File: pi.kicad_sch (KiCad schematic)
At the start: 12 parts

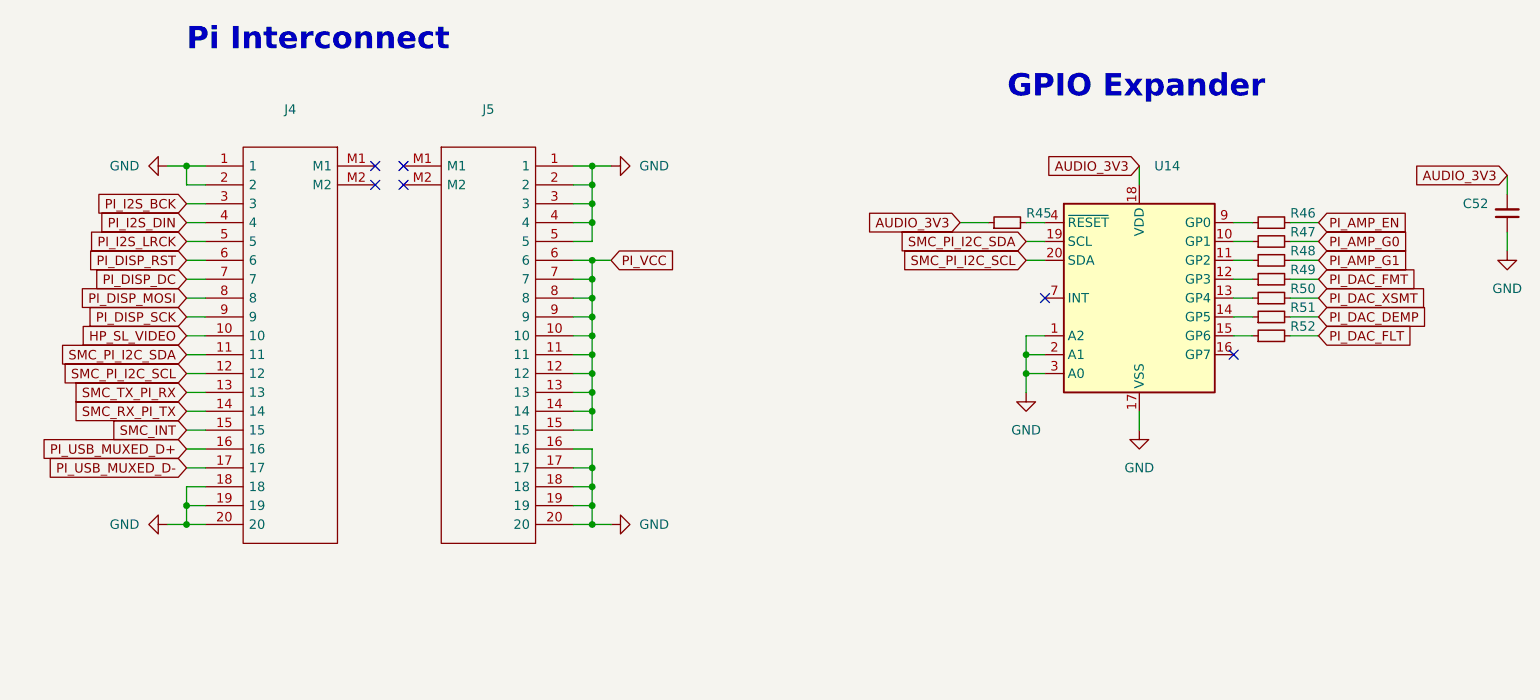
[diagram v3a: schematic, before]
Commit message: layout: update footprint for TP4056M
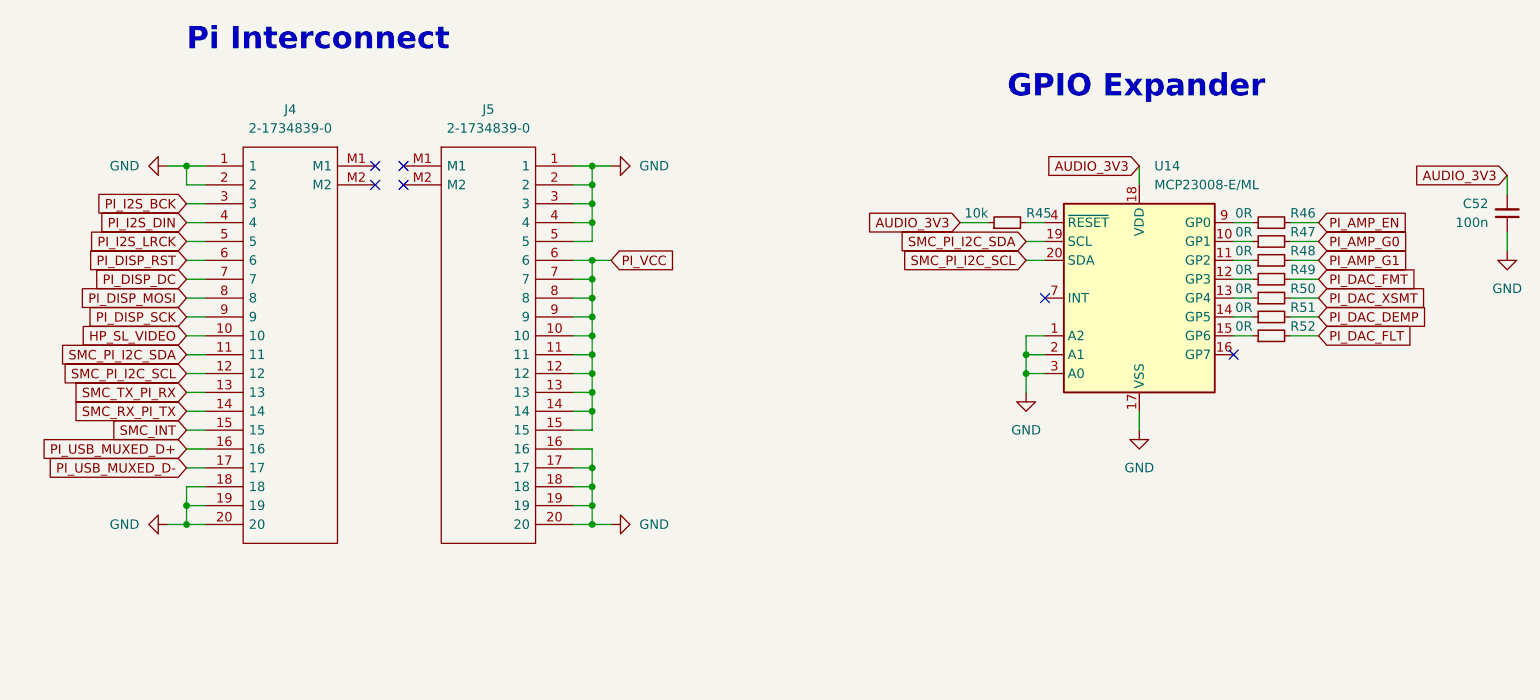
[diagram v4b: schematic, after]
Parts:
- C52: value (none) -> 100n; footprint (none) -> Capacitor_SMD:C_0402_1005Metric
- J4, J5: value (none) -> 2-1734839-0; footprint (none) -> Gigahawk:2-1734839-0
- R45: value (none) -> 10k; footprint (none) -> Resistor_SMD:R_0402_1005Metric
- R46, R47, R48, R49, R50, R51, R52: value (none) -> 0R; footprint (none) -> Resistor_SMD:R_0402_1005Metric
- U14: value (none) -> MCP23008-E/ML; footprint (none) -> Package_DFN_QFN:QFN-20-1EP_4x4mm_P0.5mm_EP2.7x2.7mm
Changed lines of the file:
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@@
       (effects (font (size 1.27 1.27)) (justify right))
     )
-    (property "Value" "" (id 1) (at 184.15 76.2 90)
-      (effects (font (size 1.27 1.27)) (justify left))
-    )
-    (property "Footprint" "" (id 2) (at 186.69 77.47 0)
+    (property "Value" "0R" (id 1) (at 184.15 76.2 90)
+      (effects (font (size 1.27 1.27)) (justify left))
+    )
+    (property "Footprint" "Resistor_SMD:R_0402_1005Metric" (id 2) (at 186.69 77.47 0)
       (effects (font (size 1.27 1.27)) hide)
     )
@@
       (effects (font (size 1.27 1.27)) (justify right))
     )
-    (property "Value" "" (id 1) (at 148.59 76.2 90)
-      (effects (font (size 1.27 1.27)) (justify left))
-    )
-    (property "Footprint" "" (id 2) (at 151.13 77.47 0)
+    (property "Value" "10k" (id 1) (at 148.59 76.2 90)
+      (effects (font (size 1.27 1.27)) (justify left))
+    )
+    (property "Footprint" "Resistor_SMD:R_0402_1005Metric" (id 2) (at 151.13 77.47 0)
       (effects (font (size 1.27 1.27)) hide)
     )
@@
       (effects (font (size 1.27 1.27)) (justify right))
     )
-    (property "Value" "" (id 1) (at 184.15 86.36 90)
-      (effects (font (size 1.27 1.27)) (justify left))
-    )
-    (property "Footprint" "" (id 2) (at 186.69 87.63 0)
+    (property "Value" "0R" (id 1) (at 184.15 86.36 90)
+      (effects (font (size 1.27 1.27)) (justify left))
+    )
+    (property "Footprint" "Resistor_SMD:R_0402_1005Metric" (id 2) (at 186.69 87.63 0)
       (effects (font (size 1.27 1.27)) hide)
     )
@@
       (effects (font (size 1.27 1.27)) (justify left))
     )
-    (property "Value" "" (id 1) (at 170.9294 72.39 0)
-      (effects (font (size 1.27 1.27)) (justify left))
-    )
-    (property "Footprint" "" (id 2) (at 168.91 114.3 0)
+    (property "Value" "MCP23008-E/ML" (id 1) (at 170.9294 72.39 0)
+      (effects (font (size 1.27 1.27)) (justify left))
+    )
+    (property "Footprint" "Package_DFN_QFN:QFN-20-1EP_4x4mm_P0.5mm_EP2.7x2.7mm" (id 2) (at 168.91 114.3 0)
       (effects (font (size 1.27 1.27)) hide)
     )
@@
     (in_bom yes) (on_board yes) (fields_autoplaced)
     (property "Reference" "J4" (id 0) (at 54.61 62.23 0))
-    (property "Value" "" (id 1) (at 54.61 64.77 0))
-    (property "Footprint" "" (id 2) (at 46.99 67.31 0)
+    (property "Value" "2-1734839-0" (id 1) (at 54.61 64.77 0))
+    (property "Footprint" "Gigahawk:2-1734839-0" (id 2) (at 46.99 67.31 0)
       (effects (font (size 1.27 1.27)) (justify left) hide)
     )
@@
     (in_bom yes) (on_board yes) (fields_autoplaced)
     (property "Reference" "J5" (id 0) (at 81.28 62.23 0))
-    (property "Value" "" (id 1) (at 81.28 64.77 0))
-    (property "Footprint" "" (id 2) (at 88.9 67.31 0)
+    (property "Value" "2-1734839-0" (id 1) (at 81.28 64.77 0))
+    (property "Footprint" "Gigahawk:2-1734839-0" (id 2) (at 88.9 67.31 0)
       (effects (font (size 1.27 1.27)) (justify left) hide)
     )
@@
       (effects (font (size 1.27 1.27)) (justify right))
     )
-    (property "Value" "" (id 1) (at 184.15 91.44 90)
-      (effects (font (size 1.27 1.27)) (justify left))
-    )
-    (property "Footprint" "" (id 2) (at 186.69 92.71 0)
+    (property "Value" "0R" (id 1) (at 184.15 91.44 90)
+      (effects (font (size 1.27 1.27)) (justify left))
+    )
+    (property "Footprint" "Resistor_SMD:R_0402_1005Metric" (id 2) (at 186.69 92.71 0)
       (effects (font (size 1.27 1.27)) hide)
     )
@@
       (effects (font (size 1.27 1.27)) (justify right))
     )
-    (property "Value" "" (id 1) (at 184.15 83.82 90)
-      (effects (font (size 1.27 1.27)) (justify left))
-    )
-    (property "Footprint" "" (id 2) (at 186.69 85.09 0)
+    (property "Value" "0R" (id 1) (at 184.15 83.82 90)
+      (effects (font (size 1.27 1.27)) (justify left))
+    )
+    (property "Footprint" "Resistor_SMD:R_0402_1005Metric" (id 2) (at 186.69 85.09 0)
       (effects (font (size 1.27 1.27)) hide)
     )
@@
       (effects (font (size 1.27 1.27)) (justify right))
     )
-    (property "Value" "" (id 1) (at 215.9 77.4635 0)
-      (effects (font (size 1.27 1.27)) (justify right))
-    )
-    (property "Footprint" "" (id 2) (at 218.44 76.2 0)
+    (property "Value" "100n" (id 1) (at 215.9 77.4635 0)
+      (effects (font (size 1.27 1.27)) (justify right))
+    )
+    (property "Footprint" "Capacitor_SMD:C_0402_1005Metric" (id 2) (at 218.44 76.2 0)
       (effects (font (size 1.27 1.27)) hide)
     )
@@
       (effects (font (size 1.27 1.27)) (justify right))
     )
-    (property "Value" "" (id 1) (at 184.15 88.9 90)
-      (effects (font (size 1.27 1.27)) (justify left))
-    )
-    (property "Footprint" "" (id 2) (at 186.69 90.17 0)
+    (property "Value" "0R" (id 1) (at 184.15 88.9 90)
+      (effects (font (size 1.27 1.27)) (justify left))
+    )
+    (property "Footprint" "Resistor_SMD:R_0402_1005Metric" (id 2) (at 186.69 90.17 0)
       (effects (font (size 1.27 1.27)) hide)
     )
@@
       (effects (font (size 1.27 1.27)) (justify right))
     )
-    (property "Value" "" (id 1) (at 184.15 78.74 90)
-      (effects (font (size 1.27 1.27)) (justify left))
-    )
-    (property "Footprint" "" (id 2) (at 186.69 80.01 0)
+    (property "Value" "0R" (id 1) (at 184.15 78.74 90)
+      (effects (font (size 1.27 1.27)) (justify left))
+    )
+    (property "Footprint" "Resistor_SMD:R_0402_1005Metric" (id 2) (at 186.69 80.01 0)
       (effects (font (size 1.27 1.27)) hide)
     )
@@
       (effects (font (size 1.27 1.27)) (justify right))
     )
-    (property "Value" "" (id 1) (at 184.15 81.28 90)
-      (effects (font (size 1.27 1.27)) (justify left))
-    )
-    (property "Footprint" "" (id 2) (at 186.69 82.55 0)
-      (effects (font (size 1.27 1.27)) hide)
-    )
+    (property "Value" "0R" (id 1) (at 184.15 81.28 90)
+      (effects (font (size 1.27 1.27)) (justify left))
+    )
+    (property "Footprint" "Resistor_SMD:R_0402_1005Metric" (id 2) (at 186.69 82.55 0)
+      (effects (font (size 1.27 1.27)) hide)
+    )

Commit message: layout: preliminary layout of most of board
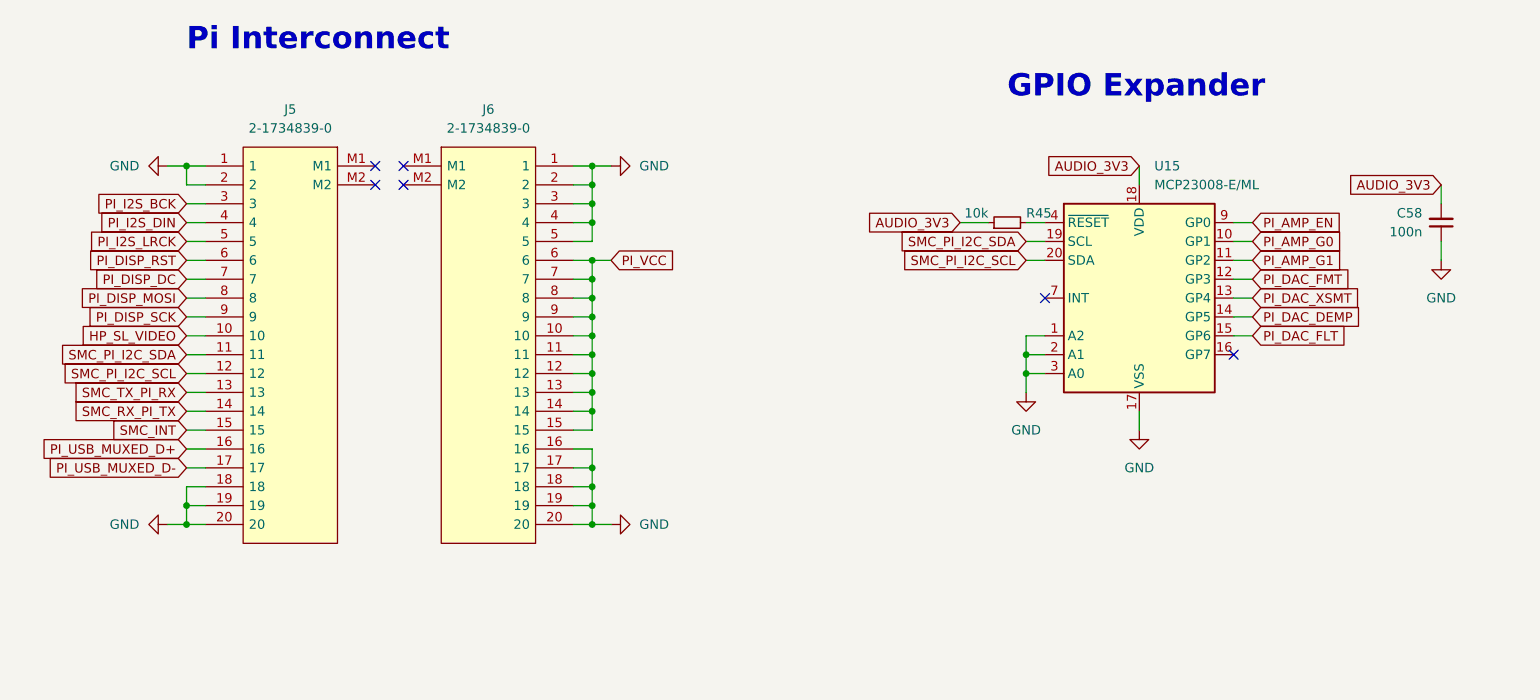
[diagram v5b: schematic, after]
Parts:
- removed R46, R47, R48, R49, R50, R51, R52: 0R, Resistor_SMD:R_0402_1005Metric, symbol Device:R_Small
- renumbered C52 to C58, J4 to J5, J5 to J6, U14 to U15
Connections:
- net PI_AMP_EN: now also U15.9 (GP0)
- net PI_AMP_G0: now also U15.10 (GP1)
- net PI_AMP_G1: now also U15.11 (GP2)
- net PI_DAC_DEMP: now also U15.14 (GP5)
- net PI_DAC_FLT: now also U15.15 (GP6)
- net PI_DAC_FMT: now also U15.12 (GP3)
- net PI_DAC_XSMT: now also U15.13 (GP4)
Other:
- moved on the sheet: C58

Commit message: routing: begin routing
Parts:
- removed J5, J6: 2-1734839-0, Gigahawk:2-1734839-0, symbol gigahawk:2-1734839-0
- added J5: (no value), symbol gigahawk:2-1734839-5
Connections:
- net GND: now also J5.24, J5.25, J5.6, J5.7, J5.8
- net HP_SL_VIDEO: now also J5.16
- net PI_DISP_DC: now also J5.19
- net PI_DISP_MOSI: now also J5.18
- net PI_DISP_RST: now also J5.20
- net PI_DISP_SCK: now also J5.17
- net PI_I2S_BCK: now also J5.22
- net PI_I2S_DIN: now also J5.21
- net PI_I2S_LRCK: now also J5.23
- net PI_USB_MUXED_D+: now also J5.10
- net PI_USB_MUXED_D-: now also J5.9
- net PI_VCC: now also J5.1, J5.2, J5.3, J5.4, J5.5
- net SMC_INT: now also J5.11
- net SMC_PI_I2C_SCL: now also J5.14
- net SMC_PI_I2C_SDA: now also J5.15
- net SMC_RX_PI_TX: now also J5.13
- net SMC_TX_PI_RX: now also J5.12
- no-connect marks 6 -> 4

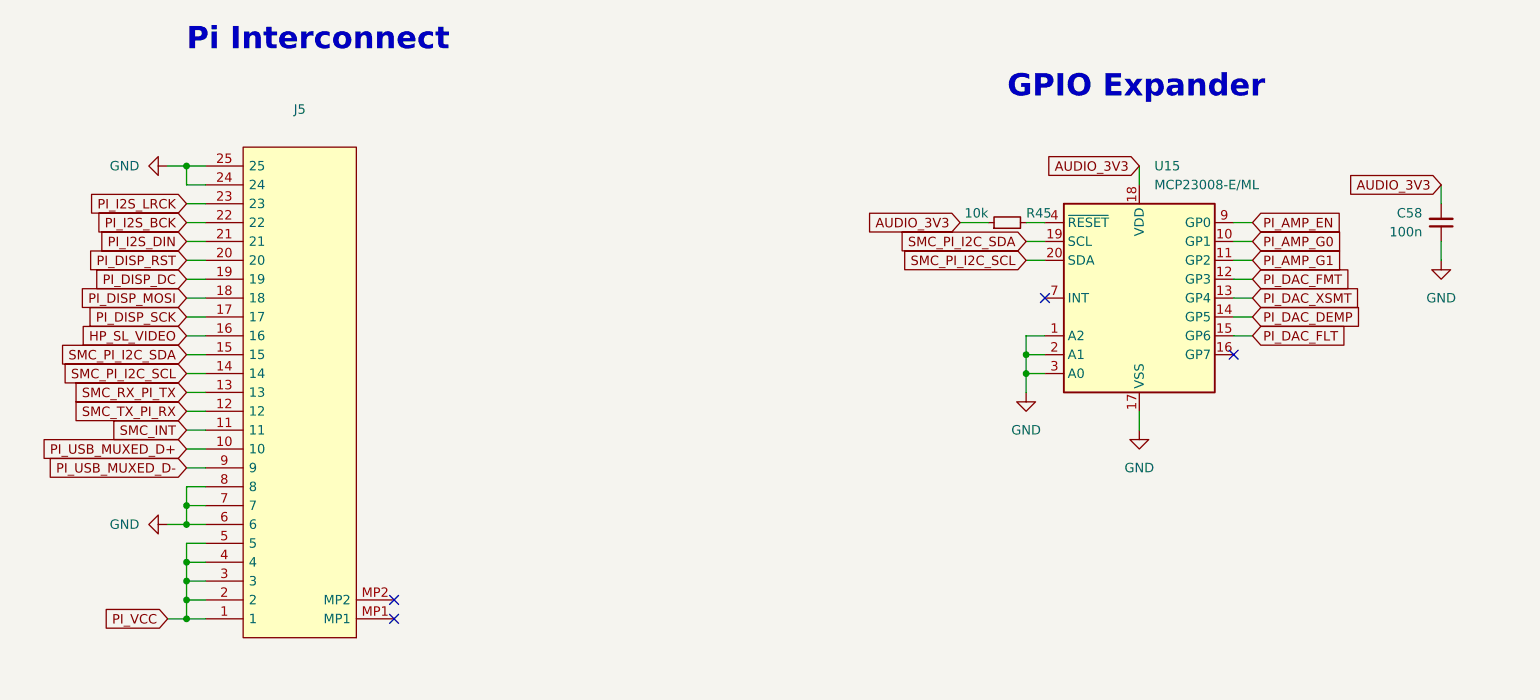
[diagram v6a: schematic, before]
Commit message: routing: finish routing (board is not manufacturable)
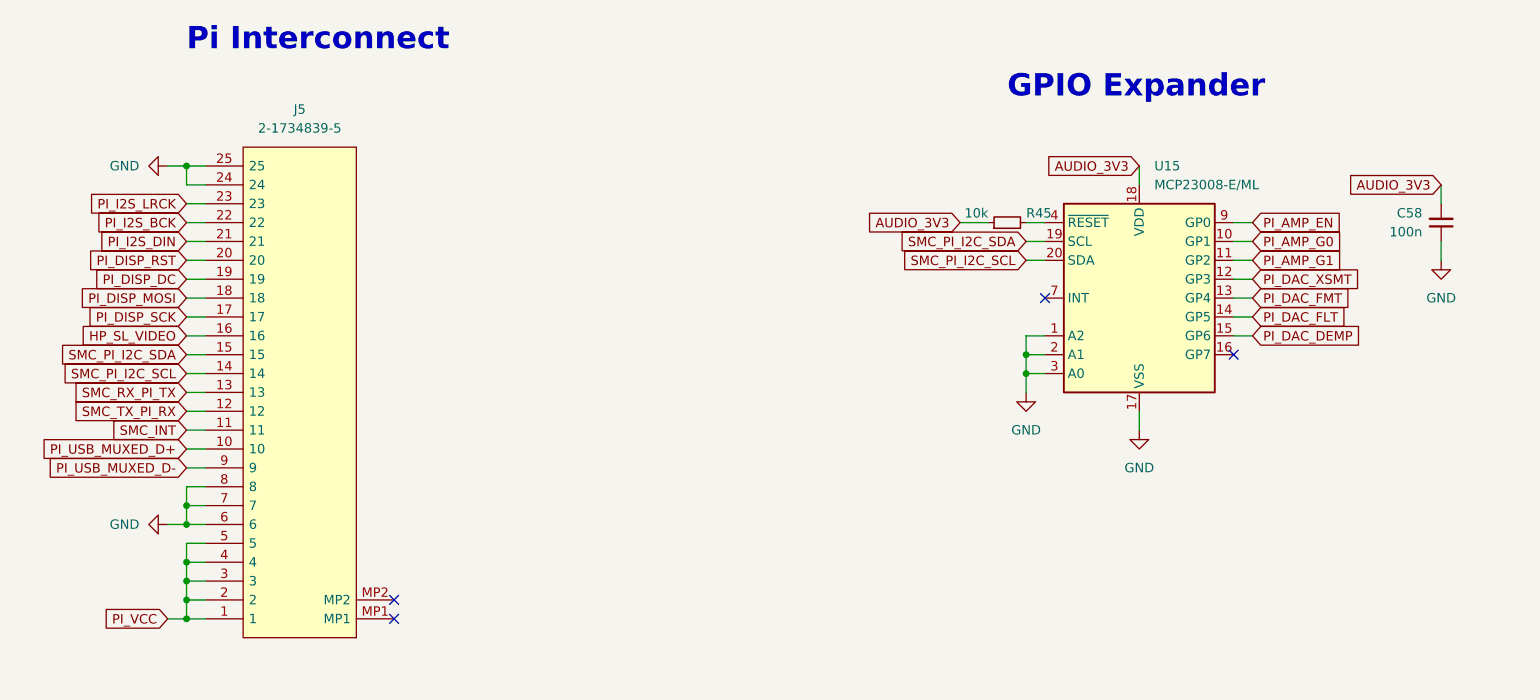
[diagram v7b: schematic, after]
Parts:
- J5: value (none) -> 2-1734839-5; footprint (none) -> Gigahawk:217348395
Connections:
- net PI_DAC_DEMP: now also U15.15 (GP6); no longer U15.14 (GP5)
- net PI_DAC_FLT: now also U15.14 (GP5); no longer U15.15 (GP6)
- net PI_DAC_FMT: now also U15.13 (GP4); no longer U15.12 (GP3)
- net PI_DAC_XSMT: now also U15.12 (GP3); no longer U15.13 (GP4)
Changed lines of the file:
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@@
     )
   )
-  (global_label "PI_DAC_DEMP" (shape input) (at 184.15 90.17 0) (fields_autoplaced)
-    (effects (font (size 1.27 1.27)) (justify left))
-    (property "Intersheet References" "${INTERSHEET_REFS}" (id 0) (at 199.1421 90.2494 0)
+  (global_label "PI_DAC_DEMP" (shape input) (at 184.15 92.71 0) (fields_autoplaced)
+    (effects (font (size 1.27 1.27)) (justify left))
+    (property "Intersheet References" "${INTERSHEET_REFS}" (id 0) (at 199.1421 92.7894 0)
       (effects (font (size 1.27 1.27)) (justify left) hide)
     )
@@
     )
   )
-  (global_label "PI_DAC_FMT" (shape input) (at 184.15 85.09 0) (fields_autoplaced)
-    (effects (font (size 1.27 1.27)) (justify left))
-    (property "Intersheet References" "${INTERSHEET_REFS}" (id 0) (at 197.5093 85.1694 0)
-      (effects (font (size 1.27 1.27)) (justify left) hide)
-    )
-  )
-  (global_label "PI_DAC_XSMT" (shape input) (at 184.15 87.63 0) (fields_autoplaced)
-    (effects (font (size 1.27 1.27)) (justify left))
-    (property "Intersheet References" "${INTERSHEET_REFS}" (id 0) (at 198.8398 87.7094 0)
-      (effects (font (size 1.27 1.27)) (justify left) hide)
-    )
-  )
-  (global_label "PI_DAC_FLT" (shape input) (at 184.15 92.71 0) (fields_autoplaced)
-    (effects (font (size 1.27 1.27)) (justify left))
-    (property "Intersheet References" "${INTERSHEET_REFS}" (id 0) (at 197.086 92.7894 0)
+  (global_label "PI_DAC_FMT" (shape input) (at 184.15 87.63 0) (fields_autoplaced)
+    (effects (font (size 1.27 1.27)) (justify left))
+    (property "Intersheet References" "${INTERSHEET_REFS}" (id 0) (at 197.5093 87.7094 0)
+      (effects (font (size 1.27 1.27)) (justify left) hide)
+    )
+  )
+  (global_label "PI_DAC_XSMT" (shape input) (at 184.15 85.09 0) (fields_autoplaced)
+    (effects (font (size 1.27 1.27)) (justify left))
+    (property "Intersheet References" "${INTERSHEET_REFS}" (id 0) (at 198.8398 85.1694 0)
+      (effects (font (size 1.27 1.27)) (justify left) hide)
+    )
+  )
+  (global_label "PI_DAC_FLT" (shape input) (at 184.15 90.17 0) (fields_autoplaced)
+    (effects (font (size 1.27 1.27)) (justify left))
+    (property "Intersheet References" "${INTERSHEET_REFS}" (id 0) (at 197.086 90.2494 0)
       (effects (font (size 1.27 1.27)) (justify left) hide)
     )
@@
     (in_bom yes) (on_board yes) (fields_autoplaced)
     (property "Reference" "J5" (id 0) (at 55.88 62.23 0))
-    (property "Value" "" (id 1) (at 55.88 64.77 0))
-    (property "Footprint" "" (id 2) (at 46.99 133.35 0)
-      (effects (font (size 1.27 1.27)) (justify left) hide)
-    )
+    (property "Value" "2-1734839-5" (id 1) (at 55.88 64.77 0))
+    (property "Footprint" "Gigahawk:217348395" (id 2) (at 46.99 133.35 0)
+      (effects (font (size 1.27 1.27)) (justify left) hide)
+    )

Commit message: layout, routing: relayout and reroute board
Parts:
- C58: value 100n -> (none); footprint Capacitor_SMD:C_0402_1005Metric -> (none)
- J5: value 2-1734839-5 -> (none); footprint Gigahawk:217348395 -> (none)
- R45: value 10k -> (none); footprint Resistor_SMD:R_0402_1005Metric -> (none)
- U15: value MCP23008-E/ML -> (none); footprint Package_DFN_QFN:QFN-20-1EP_4x4mm_P0.5mm_EP2.7x2.7mm -> (none)
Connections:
- net PI_AMP_G0: now also U15.11 (GP2); no longer U15.10 (GP1)
- net PI_AMP_G1: now also U15.10 (GP1); no longer U15.11 (GP2)
- net PI_I2S_BCK: now also J5.23; no longer J5.22
- net PI_I2S_DIN: now also J5.22; no longer J5.21
- net PI_I2S_LRCK: now also J5.21; no longer J5.23
- net SMC_PI_I2C_SCL: now also J5.15; no longer J5.14
- net SMC_PI_I2C_SDA: now also J5.14; no longer J5.15
- net SMC_RX_PI_TX: now also J5.12; no longer J5.13
- net SMC_TX_PI_RX: now also J5.13; no longer J5.12
- net ~{IO_EX_RST}: now reaches R45.2, U15.4 (~{RESET})
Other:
- moved on the sheet: R45
